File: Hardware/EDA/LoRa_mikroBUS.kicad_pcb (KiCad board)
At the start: 4 copper layers, 25.4 x 28.6 mm, 7 parts, among them J1 u.FL, J2 SMA, P1 HEADER_M_2.54MM_1R8P_ST_AU_PTH, P2 HEADER_M_2.54MM_1R8P_ST_AU_PTH, U1 RFM95W

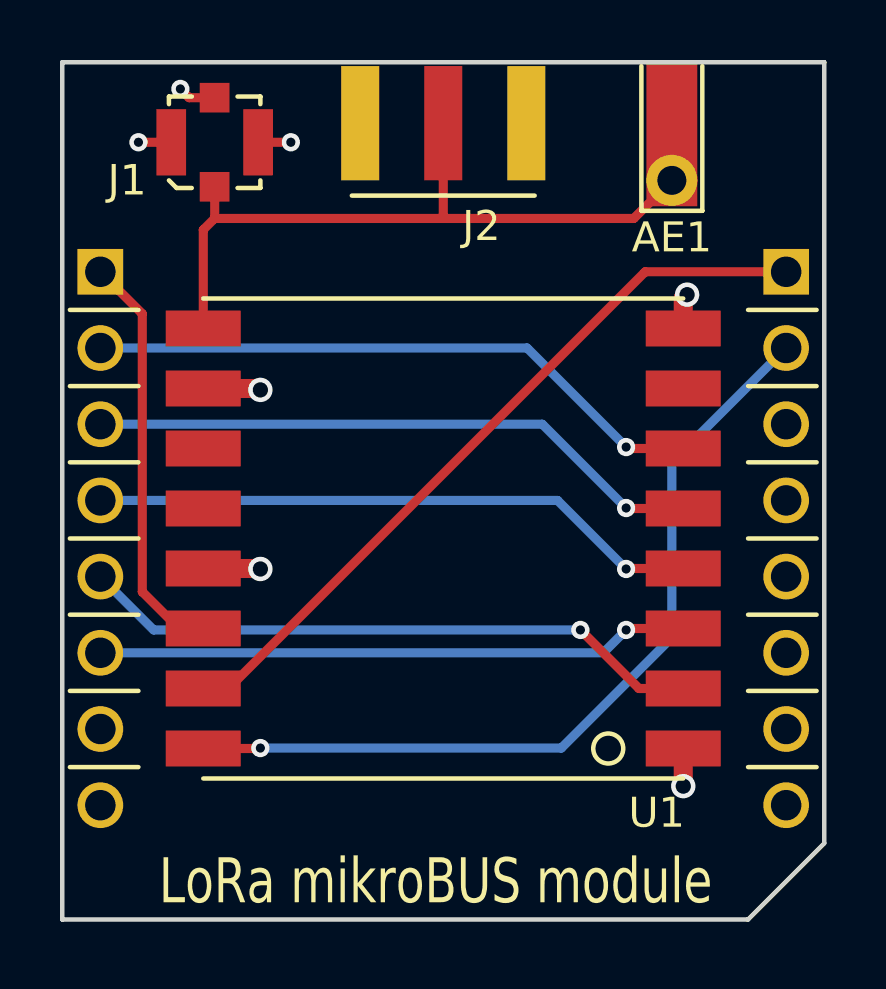
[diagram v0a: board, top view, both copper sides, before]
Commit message: Added ground connections to SMA edge connector.  Removed extra *.pro file in parent directory.
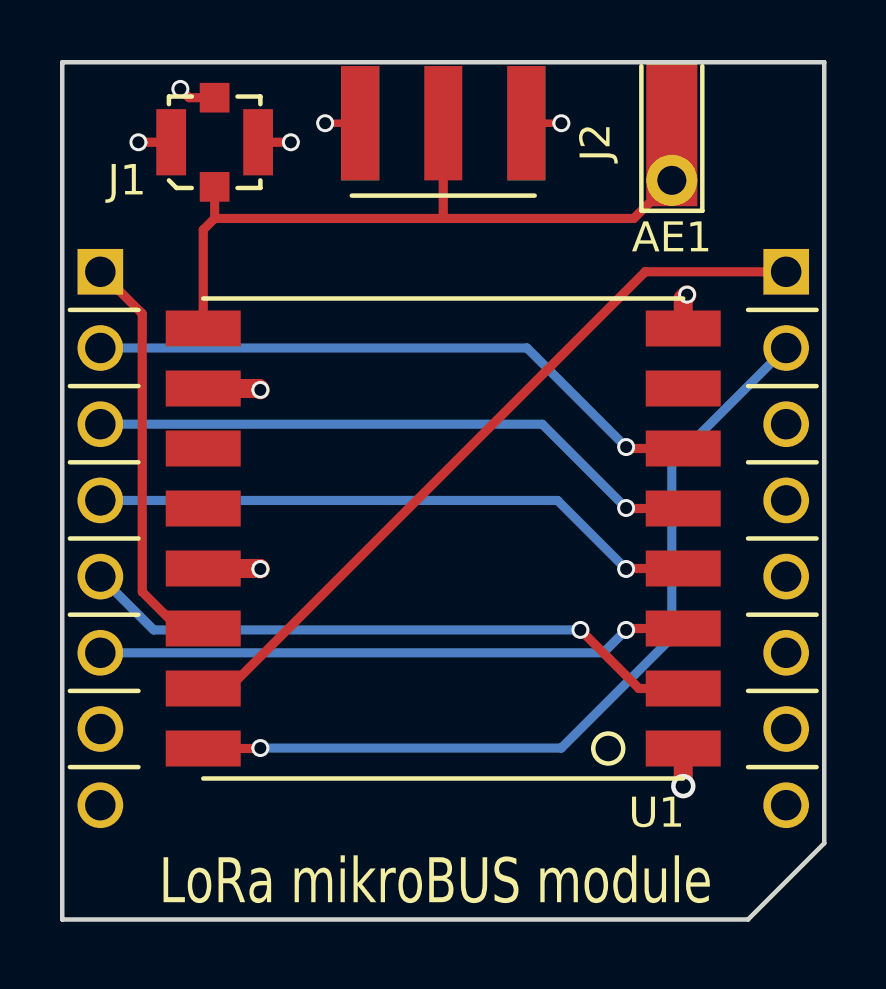
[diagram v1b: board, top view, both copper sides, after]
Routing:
- net GND: track 7.81 -> 10.1 mm, vias 6 -> 8
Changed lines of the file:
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@@
     (links 22)
     (no_connects 0)
-    (area 110.922999 97.714999 136.473001 126.440001)
+    (area 110.696399 97.467 136.699601 127.838023)
     (thickness 1.6)
     (drawings 40)
-    (tracks 65)
+    (tracks 69)
     (zones 0)
     (modules 7)
@@
       (net 12 INT))
     (model C:/Engineering/KiCAD_Libraries/3D/Modules/VRML/RFM95W.wrl
-      (at (xyz 0 0 0))
-      (scale (xyz 1 1 1))
-      (rotate (xyz 0 0 0))
-    )
-  )
-  (module Connector:SMA_EDGE (layer F.Cu)
-    (at 123.698 97.917 270)
-    (fp_text reference J2 (at 5.334 -1.27 360) (layer F.SilkS)
-      (effects (font (size 1 1) (thickness 0.15)))
-    )
-    (fp_text value SMA (at 1.27 12.065 360) (layer F.Fab) hide
-      (effects (font (size 1 1) (thickness 0.15)))
-    )
-    (fp_line (start 4.318 -3.048) (end 4.318 3.048) (layer F.SilkS) (width 0.15))
-    (pad 2 smd rect (at 1.905 -2.7686 270) (size 3.81 1.27) (layers *.Cu F.Paste F.Mask)
-      (net 7 GND))
-    (pad 3 smd rect (at 1.905 2.7686 270) (size 3.81 1.27) (layers *.Cu F.Paste F.Mask)
-      (net 7 GND))
-    (pad 1 smd rect (at 1.905 0 270) (size 3.81 1.27) (layers F.Cu F.Paste F.Mask)
-      (net 19 "Net-(AE1-Pad1)"))
-    (model C:/Engineering/KiCAD_Libraries/3D/Connectors/RF/VRML/SMA_EDGE.wrl
       (at (xyz 0 0 0))
       (scale (xyz 1 1 1))
@@
       (net 19 "Net-(AE1-Pad1)"))
   )
+  (module Connector:SMA_EDGE (layer F.Cu)
+    (at 123.698 97.917 270)
+    (fp_text reference J2 (at 2.54 -5.08 270) (layer F.SilkS)
+      (effects (font (size 1 1) (thickness 0.15)))
+    )
+    (fp_text value SMA (at 3.81 5.08 270) (layer F.Fab)
+      (effects (font (size 1 1) (thickness 0.15)))
+    )
+    (fp_line (start 4.318 -3.048) (end 4.318 3.048) (layer F.SilkS) (width 0.15))
+    (pad "" smd rect (at 1.905 2.7686 270) (size 3.81 1.27) (layers B.Cu))
+    (pad "" smd rect (at 1.905 -2.7686 270) (size 3.81 1.27) (layers B.Cu))
+    (pad 2 smd rect (at 1.905 -2.7686 270) (size 3.81 1.27) (layers F.Cu)
+      (net 7 GND))
+    (pad 3 smd rect (at 1.905 2.7686 270) (size 3.81 1.27) (layers F.Cu)
+      (net 7 GND))
+    (pad 1 smd rect (at 1.905 0 270) (size 3.81 1.27) (layers F.Cu F.Paste F.Mask)
+      (net 19 "Net-(AE1-Pad1)"))
+    (model C:/Engineering/KiCAD_Libraries/3D/Connectors/RF/VRML/SMA_EDGE.wrl
+      (at (xyz 0 0 0))
+      (scale (xyz 1 1 1))
+      (rotate (xyz 0 0 0))
+    )
+  )
   (gr_line (start 133.858 126.365) (end 136.398 123.825) (angle 90) (layer Edge.Cuts) (width 0.15))
   (gr_text CS (at 115.189 109.982) (layer B.SilkS)
@@
   (segment (start 129.842 116.665) (end 131.698 116.665) (width 0.3048) (layer F.Cu) (net 1))
   (segment (start 129.794 116.713) (end 129.842 116.665) (width 0.3048) (layer F.Cu) (net 1))
-  (via (at 129.794 116.713) (size 0.6096) (drill 0.3048) (layers F.Cu B.Cu) (net 1))
+  (via (at 129.794 116.713) (size 0.6) (drill 0.4) (layers F.Cu B.Cu) (net 1))
   (segment (start 129.032 117.475) (end 129.794 116.713) (width 0.3048) (layer B.Cu) (net 1))
   (segment (start 131.698 114.665) (end 129.81 114.665) (width 0.3048) (layer F.Cu) (net 2))
   (segment (start 127.508 112.395) (end 112.268 112.395) (width 0.3048) (layer B.Cu) (net 2))
   (segment (start 129.794 114.681) (end 127.508 112.395) (width 0.3048) (layer B.Cu) (net 2))
-  (via (at 129.794 114.681) (size 0.6096) (drill 0.3048) (layers F.Cu B.Cu) (net 2))
+  (via (at 129.794 114.681) (size 0.6) (drill 0.4) (layers F.Cu B.Cu) (net 2))
   (segment (start 129.81 114.665) (end 129.794 114.681) (width 0.3048) (layer F.Cu) (net 2))
   (segment (start 112.268 109.855) (end 127 109.855) (width 0.3048) (layer B.Cu) (net 3))
   (segment (start 129.81 112.665) (end 131.698 112.665) (width 0.3048) (layer F.Cu) (net 3))
   (segment (start 129.794 112.649) (end 129.81 112.665) (width 0.3048) (layer F.Cu) (net 3))
-  (via (at 129.794 112.649) (size 0.6096) (drill 0.3048) (layers F.Cu B.Cu) (net 3))
+  (via (at 129.794 112.649) (size 0.6) (drill 0.4) (layers F.Cu B.Cu) (net 3))
   (segment (start 127 109.855) (end 129.794 112.649) (width 0.3048) (layer B.Cu) (net 3))
   (segment (start 131.698 110.665) (end 129.842 110.665) (width 0.3048) (layer F.Cu) (net 4))
   (segment (start 126.492 107.315) (end 112.268 107.315) (width 0.3048) (layer B.Cu) (net 4))
   (segment (start 129.794 110.617) (end 126.492 107.315) (width 0.3048) (layer B.Cu) (net 4))
-  (via (at 129.794 110.617) (size 0.6096) (drill 0.3048) (layers F.Cu B.Cu) (net 4))
+  (via (at 129.794 110.617) (size 0.6) (drill 0.4) (layers F.Cu B.Cu) (net 4))
   (segment (start 129.842 110.665) (end 129.794 110.617) (width 0.3048) (layer F.Cu) (net 4))
   (segment (start 115.698 116.665) (end 114.887 116.665) (width 0.3048) (layer F.Cu) (net 5))
@@
   (segment (start 113.665 106.172) (end 112.268 104.775) (width 0.3048) (layer F.Cu) (net 5))
   (segment (start 115.698 114.665) (end 117.586 114.665) (width 0.635) (layer F.Cu) (net 6))
-  (via (at 117.602 114.681) (size 0.8128) (drill 0.508) (layers F.Cu B.Cu) (net 6))
+  (via (at 117.602 114.681) (size 0.6) (drill 0.4) (layers F.Cu B.Cu) (net 6))
   (segment (start 117.586 114.665) (end 117.602 114.681) (width 0.635) (layer F.Cu) (net 6))
+  (segment (start 126.4666 99.822) (end 127.635 99.822) (width 0.25) (layer F.Cu) (net 7))
+  (via (at 127.635 99.822) (size 0.6) (drill 0.4) (layers F.Cu B.Cu) (net 7))
+  (segment (start 120.9294 99.822) (end 119.761 99.822) (width 0.25) (layer F.Cu) (net 7))
+  (via (at 119.761 99.822) (size 0.6) (drill 0.4) (layers F.Cu B.Cu) (net 7))
   (segment (start 131.698 106.665) (end 131.698 105.665) (width 0.635) (layer F.Cu) (net 7))
-  (via (at 131.826 105.537) (size 0.8128) (drill 0.508) (layers F.Cu B.Cu) (net 7))
+  (via (at 131.826 105.537) (size 0.6) (drill 0.4) (layers F.Cu B.Cu) (net 7))
   (segment (start 131.698 105.665) (end 131.826 105.537) (width 0.635) (layer F.Cu) (net 7))
   (segment (start 115.698 108.665) (end 117.555 108.665) (width 0.635) (layer F.Cu) (net 7))
-  (via (at 117.602 108.712) (size 0.8128) (drill 0.508) (layers F.Cu B.Cu) (net 7))
+  (via (at 117.602 108.712) (size 0.6) (drill 0.4) (layers F.Cu B.Cu) (net 7))
   (segment (start 117.555 108.665) (end 117.602 108.712) (width 0.635) (layer F.Cu) (net 7))
   (segment (start 131.698 120.665) (end 131.698 121.919) (width 0.635) (layer F.Cu) (net 7))
@@
   (segment (start 131.698 121.919) (end 131.699 121.92) (width 0.635) (layer F.Cu) (net 7))
   (segment (start 117.5258 100.457) (end 118.618 100.457) (width 0.3048) (layer F.Cu) (net 7))
-  (via (at 118.618 100.457) (size 0.6096) (drill 0.3048) (layers F.Cu B.Cu) (net 7))
+  (via (at 118.618 100.457) (size 0.6) (drill 0.4) (layers F.Cu B.Cu) (net 7))
   (segment (start 116.078 98.9711) (end 115.2271 98.9711) (width 0.3048) (layer F.Cu) (net 7))
-  (via (at 114.935 98.679) (size 0.6096) (drill 0.3048) (layers F.Cu B.Cu) (net 7))
+  (via (at 114.935 98.679) (size 0.6) (drill 0.4) (layers F.Cu B.Cu) (net 7))
   (segment (start 115.2271 98.9711) (end 114.935 98.679) (width 0.3048) (layer F.Cu) (net 7))
   (segment (start 114.6302 100.457) (end 113.538 100.457) (width 0.3048) (layer F.Cu) (net 7))
-  (via (at 113.538 100.457) (size 0.6096) (drill 0.3048) (layers F.Cu B.Cu) (net 7))
+  (via (at 113.538 100.457) (size 0.6) (drill 0.4) (layers F.Cu B.Cu) (net 7))
   (segment (start 112.268 114.935) (end 114.046 116.713) (width 0.3048) (layer B.Cu) (net 8))
   (segment (start 130.222 118.665) (end 131.698 118.665) (width 0.3048) (layer F.Cu) (net 8))
   (segment (start 128.27 116.713) (end 130.222 118.665) (width 0.3048) (layer F.Cu) (net 8))
-  (via (at 128.27 116.713) (size 0.6096) (drill 0.3048) (layers F.Cu B.Cu) (net 8))
+  (via (at 128.27 116.713) (size 0.6) (drill 0.4) (layers F.Cu B.Cu) (net 8))
   (segment (start 114.046 116.713) (end 128.27 116.713) (width 0.3048) (layer B.Cu) (net 8))
   (segment (start 135.128 107.315) (end 131.318 111.125) (width 0.3048) (layer B.Cu) (net 12))
   (segment (start 117.587 120.665) (end 115.698 120.665) (width 0.3048) (layer F.Cu) (net 12))
   (segment (start 117.602 120.65) (end 117.587 120.665) (width 0.3048) (layer F.Cu) (net 12))
-  (via (at 117.602 120.65) (size 0.6096) (drill 0.3048) (layers F.Cu B.Cu) (net 12))
+  (via (at 117.602 120.65) (size 0.6) (drill 0.4) (layers F.Cu B.Cu) (net 12))
   (segment (start 127.635 120.65) (end 117.602 120.65) (width 0.3048) (layer B.Cu) (net 12))
   (segment (start 131.318 116.967) (end 127.635 120.65) (width 0.3048) (layer B.Cu) (net 12))
